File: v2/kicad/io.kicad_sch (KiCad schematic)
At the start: 9 parts, among them J1 Conn_01x10_Female, SW1 UP, SW2 DOWN, SW3 OK, SW4 CANCEL

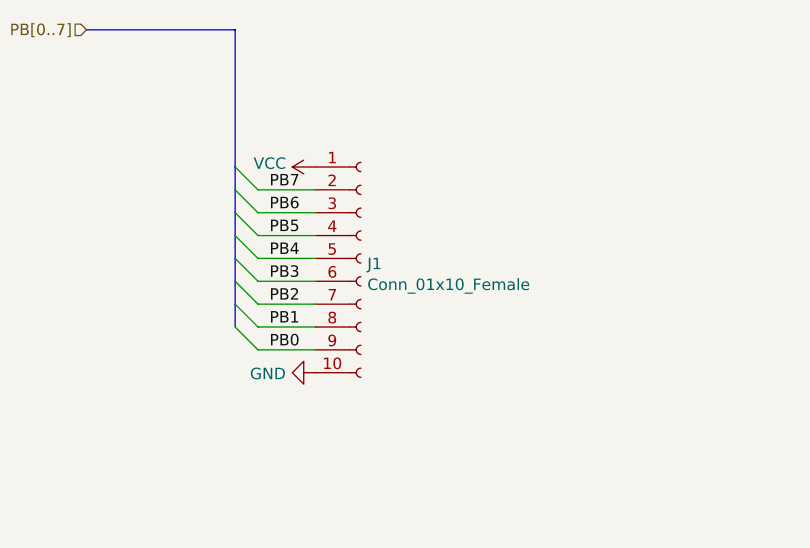
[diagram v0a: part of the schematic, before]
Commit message: PCB Tweaks
Tracks optimized.
SMD components moved to top layer.
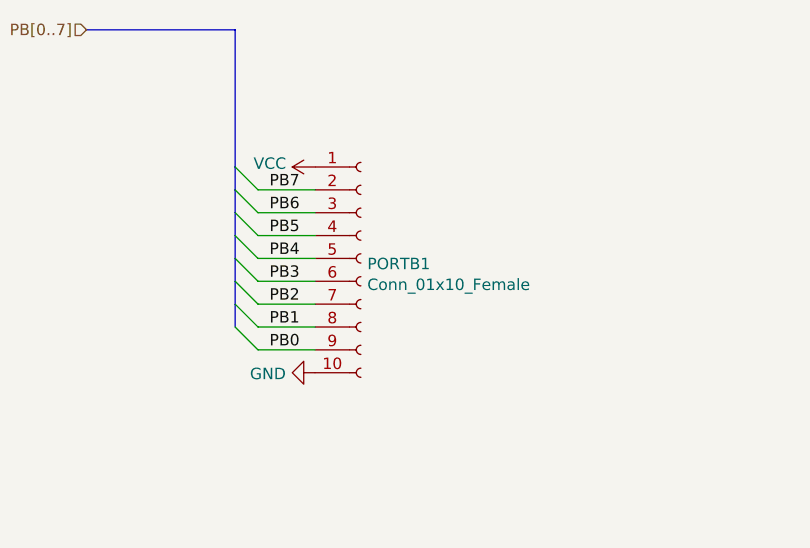
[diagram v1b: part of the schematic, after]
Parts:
- renumbered J1 to PORTB1
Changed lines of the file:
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@@
   (symbol (lib_id "Connector:Conn_01x10_Female") (at 99.06 77.47 0) (unit 1)
     (in_bom yes) (on_board yes)
-    (property "Reference" "J1" (id 0) (at 99.7712 78.0796 0)
+    (property "Reference" "PORTB1" (id 0) (at 99.7712 78.0796 0)
       (effects (font (size 1.27 1.27)) (justify left))
     )
